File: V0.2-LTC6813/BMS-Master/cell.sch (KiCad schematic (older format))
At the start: 3 parts

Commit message: schematics 50% complete3d
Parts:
- added JP?: Jumper_NC_Dual-Device, symbol BMS-Master-rescue:Jumper_NC_Dual-Device
- added Q?: BSS138, Package_TO_SOT_SMD:SOT-23, symbol Transistor_FET:BSS138
- added R?: 10, Resistor_SMD:R_0603_1608Metric_Pad0.99x1.00mm_HandSolder, symbol Device:R
- added R?: 33, Resistor_SMD:R_0603_1608Metric_Pad0.99x1.00mm_HandSolder, symbol Device:R
- C?: value C -> 100n; Voltage (none) -> 100V
- R?: value 10 -> 100
- R?: value 33 -> R
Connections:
- net C+: now also JP?.3, Q?.2 (S); no longer R?.2
- net V-: now also R?.1; no longer C?.1
- new net: JP?.2, R?.2
- new net: JP?.1, Q?.1 (G)
- new net: Q?.3 (D), R?.2
- new net GND: C?.1
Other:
- moved on the sheet: C?

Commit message: Schematics 75% completed
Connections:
- net GND renamed GNDA
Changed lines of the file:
@@
 Wire Wire Line
 	5650 3950 5650 4750
+Wire Wire Line
+	3400 4800 3400 5000
+Wire Wire Line
+	3400 5000 2550 5000
 $Comp
-L power:GND #PWR?
-U 1 1 5C6DEC90
+L power:GNDA #PWR?
+U 1 1 5C8C20A9
 P 5650 4750
-AR Path="/5B4A196B/5B5115CC/5C6DEC90" Ref="#PWR?"  Part="1"
-AR Path="/5B4A196B/5B4FCC47/5C6DEC90" Ref="#PWR?"  Part="1"
-AR Path="/5B4A196B/5B4FD503/5C6DEC90" Ref="#PWR?"  Part="1"
-AR Path="/5B4A196B/5B50012A/5C6DEC90" Ref="#PWR?"  Part="1"
-AR Path="/5B4A196B/5B502FEF/5C6DEC90" Ref="#PWR?"  Part="1"
-AR Path="/5B4A196B/5B50355C/5C6DEC90" Ref="#PWR?"  Part="1"
-AR Path="/5B4A196B/5B504105/5C6DEC90" Ref="#PWR?"  Part="1"
-AR Path="/5B4A196B/5B504814/5C6DEC90" Ref="#PWR?"  Part="1"
-AR Path="/5B4A196B/5B5050BC/5C6DEC90" Ref="#PWR?"  Part="1"
-AR Path="/5B4A196B/5B50594B/5C6DEC90" Ref="#PWR?"  Part="1"
-AR Path="/5B4A196B/5B506BB1/5C6DEC90" Ref="#PWR?"  Part="1"
-AR Path="/5B4A196B/5B507536/5C6DEC90" Ref="#PWR?"  Part="1"
-AR Path="/5B4A196B/5B50804F/5C6DEC90" Ref="#PWR?"  Part="1"
-AR Path="/5B4A196B/5B508C6C/5C6DEC90" Ref="#PWR?"  Part="1"
-AR Path="/5B4A196B/5B509A8B/5C6DEC90" Ref="#PWR?"  Part="1"
-AR Path="/5B4A196B/5B50AABA/5C6DEC90" Ref="#PWR?"  Part="1"
-AR Path="/5B4A196B/5B50EED8/5C6DEC90" Ref="#PWR?"  Part="1"
-AR Path="/5B4A196B/5B510167/5C6DEC90" Ref="#PWR?"  Part="1"
 F 0 "#PWR?" H 5650 4500 50  0001 C CNN
-F 1 "GND" H 5655 4577 50  0000 C CNN
+F 1 "GNDA" H 5655 4577 50  0000 C CNN
 F 2 "" H 5650 4750 50  0001 C CNN
 F 3 "" H 5650 4750 50  0001 C CNN
@@
 	1    0    0    -1
 $EndComp
-Wire Wire Line
-	3400 4800 3400 5000
-Wire Wire Line
-	3400 5000 2550 5000
 $EndSCHEMATC

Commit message: Schematics 90% completed
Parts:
- removed R?: 10, Resistor_SMD:R_0603_1608Metric_Pad0.99x1.00mm_HandSolder, symbol Device:R
- JP21: renamed from JP?; footprint (none) -> Pin_Headers:Pin_Header_Straight_1x03_Pitch2.54mm
- gave numbers to parts that had none: 5

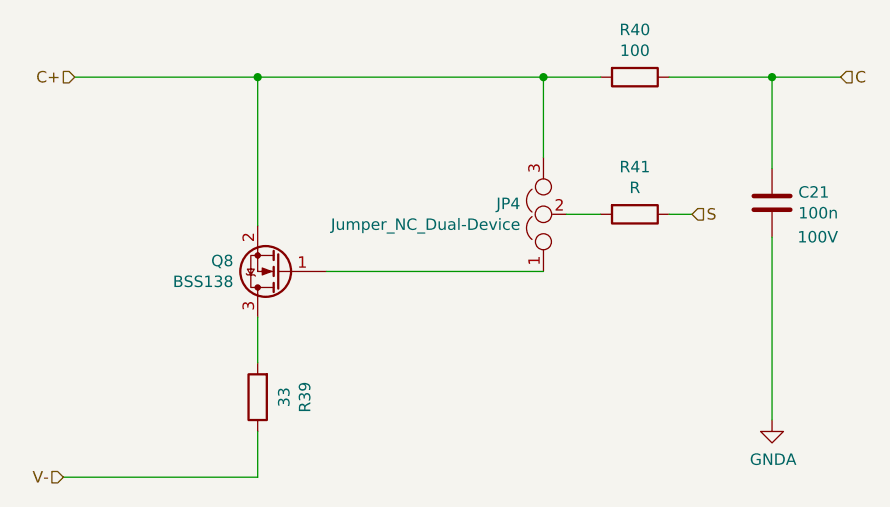
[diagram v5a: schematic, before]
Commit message: 92.5% schematics completed
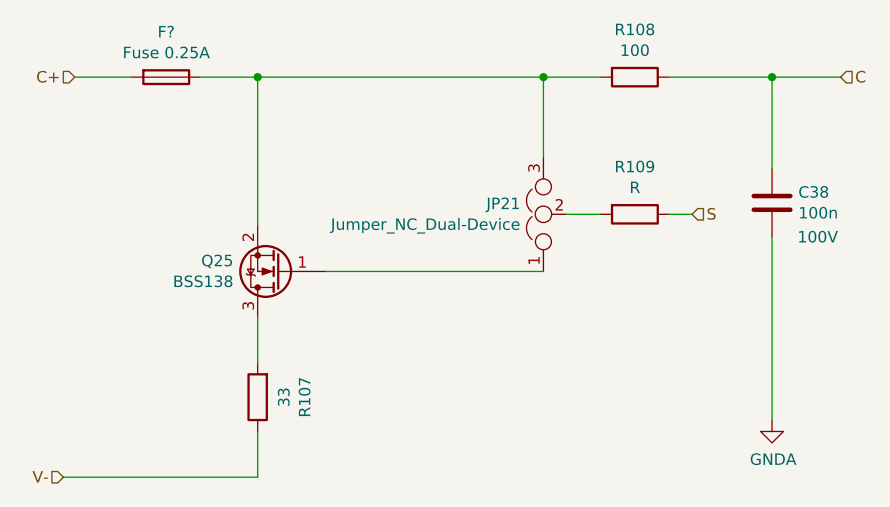
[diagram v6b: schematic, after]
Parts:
- added F?: Fuse 0.25A, Fuse_Holders_and_Fuses:Fuse_SMD1206_HandSoldering, symbol Device:Fuse
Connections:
- net C+: now also F?.2; no longer JP21.3, Q25.2 (S), R48.2
- new net: F?.1, JP21.3, Q25.2 (S), R48.2
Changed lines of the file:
@@
 AR Path="/5B4A196B/5B50EED8/5B4FCD0D" Ref="R100"  Part="1"
 AR Path="/5B4A196B/5B510167/5B4FCD0D" Ref="R104"  Part="1"
-F 0 "R40" V 4843 3250 50  0000 C CNN
+F 0 "R108" V 4843 3250 50  0000 C CNN
 F 1 "100" V 4934 3250 50  0000 C CNN
 F 2 "Resistor_SMD:R_0603_1608Metric_Pad0.99x1.00mm_HandSolder" V 4980 3250 50  0001 C CNN
@@
 AR Path="/5B4A196B/5B50EED8/5B4FCD15" Ref="C36"  Part="1"
 AR Path="/5B4A196B/5B510167/5B4FCD15" Ref="C37"  Part="1"
-F 0 "C21" H 5535 3754 50  0000 R CNN
+F 0 "C38" H 5535 3754 50  0000 R CNN
 F 1 "100n" H 5535 3845 50  0000 R CNN
 F 2 "Capacitor_SMD:C_0603_1608Metric_Pad0.99x1.00mm_HandSolder" H 5688 3650 50  0001 C CNN
@@
 AR Path="/5B4A196B/5B50EED8/5B4FCD21" Ref="R101"  Part="1"
 AR Path="/5B4A196B/5B510167/5B4FCD21" Ref="R105"  Part="1"
-F 0 "R41" V 4843 3850 50  0000 C CNN
+F 0 "R109" V 4843 3850 50  0000 C CNN
 F 1 "R" V 4934 3850 50  0000 C CNN
 F 2 "Resistor_SMD:R_0603_1608Metric_Pad0.99x1.00mm_HandSolder" V 4980 3850 50  0001 C CNN
@@
 AR Path="/5B4A196B/5B50EED8/5C6D5C4A" Ref="JP19"  Part="1"
 AR Path="/5B4A196B/5B510167/5C6D5C4A" Ref="JP20"  Part="1"
-F 0 "JP4" V 4696 3951 50  0000 L CNN
+F 0 "JP21" V 4696 3951 50  0000 L CNN
 F 1 "Jumper_NC_Dual-Device" V 4605 3951 50  0000 L CNN
 F 2 "Pin_Headers:Pin_Header_Straight_1x03_Pitch2.54mm" H 4650 3850 50  0001 C CNN
@@
 AR Path="/5B4A196B/5B50EED8/5C6D64D7" Ref="Q23"  Part="1"
 AR Path="/5B4A196B/5B510167/5C6D64D7" Ref="Q24"  Part="1"
-F 0 "Q8" H 3706 4054 50  0000 L CNN
+F 0 "Q25" H 3706 4054 50  0000 L CNN
 F 1 "BSS138" H 3706 4145 50  0000 L CNN
 F 2 "Package_TO_SOT_SMD:SOT-23" H 3700 4025 50  0001 L CIN
@@
 $EndComp
 Wire Wire Line
-	2600 3250 3400 3250
+	2600 3250 2850 3250
 Wire Wire Line
 	4650 3600 4650 3250
@@
 AR Path="/5B4A196B/5B50EED8/5C6D9E32" Ref="R99"  Part="1"
 AR Path="/5B4A196B/5B510167/5C6D9E32" Ref="R103"  Part="1"
-F 0 "R39" V 3193 4650 50  0000 C CNN
+F 0 "R107" V 3193 4650 50  0000 C CNN
 F 1 "33" V 3284 4650 50  0000 C CNN
 F 2 "Resistor_SMD:R_0603_1608Metric_Pad0.99x1.00mm_HandSolder" V 3330 4650 50  0001 C CNN
@@
 AR Path="/5B4A196B/5B510167/5C8C20A9" Ref="#PWR0170"  Part="1"
 AR Path="/5B4A196B/5B5115CC/5C8C20A9" Ref="#PWR0171"  Part="1"
-F 0 "#PWR0154" H 5650 4500 50  0001 C CNN
+F 0 "#PWR0171" H 5650 4500 50  0001 C CNN
 F 1 "GNDA" H 5655 4577 50  0000 C CNN
 F 2 "" H 5650 4750 50  0001 C CNN
@@
 Wire Wire Line
 	3400 4800 3400 5000
+Wire Wire Line
+	3150 3250 3400 3250
+$Comp
+L Device:Fuse F?
+U 1 1 5CDF9F6D
+P 3000 3250
+F 0 "F?" V 2803 3250 50  0000 C CNN
+F 1 "Fuse 0.25A" V 2894 3250 50  0000 C CNN
+F 2 "Fuse_Holders_and_Fuses:Fuse_SMD1206_HandSoldering" V 2930 3250 50  0001 C CNN
+F 3 "~" H 3000 3250 50  0001 C CNN
+	1    3000 3250
+	0    1    1    0
+$EndComp
 $EndSCHEMATC

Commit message: Schematics 99% completed
Only need to review everything &
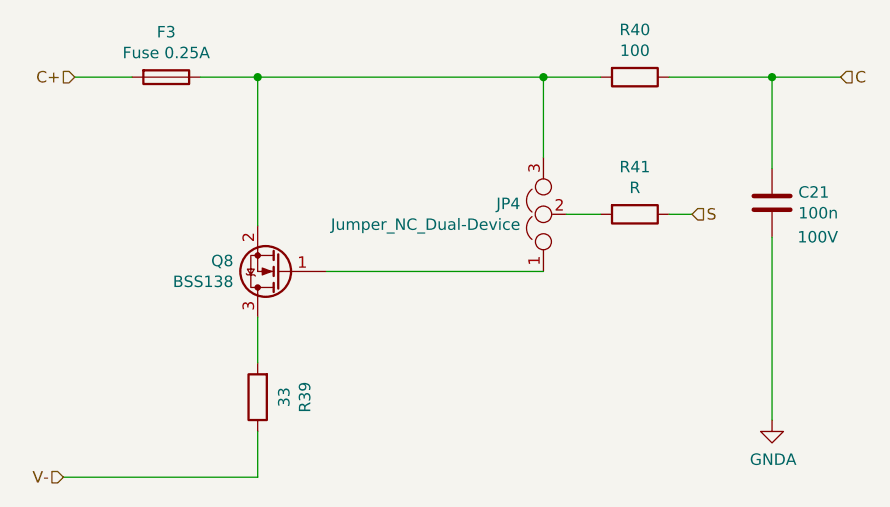
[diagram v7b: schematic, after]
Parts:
- gave numbers to parts that had none: 1
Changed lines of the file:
@@
 $Descr A4 11693 8268
 encoding utf-8
-Sheet 22 28
+Sheet 5 28
 Title ""
 Date ""
@@
 AR Path="/5B4A196B/5B50EED8/5B4FCD0D" Ref="R100"  Part="1"
 AR Path="/5B4A196B/5B510167/5B4FCD0D" Ref="R104"  Part="1"
-F 0 "R108" V 4843 3250 50  0000 C CNN
+F 0 "R40" V 4843 3250 50  0000 C CNN
 F 1 "100" V 4934 3250 50  0000 C CNN
 F 2 "Resistor_SMD:R_0603_1608Metric_Pad0.99x1.00mm_HandSolder" V 4980 3250 50  0001 C CNN
@@
 AR Path="/5B4A196B/5B50EED8/5B4FCD15" Ref="C36"  Part="1"
 AR Path="/5B4A196B/5B510167/5B4FCD15" Ref="C37"  Part="1"
-F 0 "C38" H 5535 3754 50  0000 R CNN
+F 0 "C21" H 5535 3754 50  0000 R CNN
 F 1 "100n" H 5535 3845 50  0000 R CNN
 F 2 "Capacitor_SMD:C_0603_1608Metric_Pad0.99x1.00mm_HandSolder" H 5688 3650 50  0001 C CNN
@@
 AR Path="/5B4A196B/5B50EED8/5B4FCD21" Ref="R101"  Part="1"
 AR Path="/5B4A196B/5B510167/5B4FCD21" Ref="R105"  Part="1"
-F 0 "R109" V 4843 3850 50  0000 C CNN
+F 0 "R41" V 4843 3850 50  0000 C CNN
 F 1 "R" V 4934 3850 50  0000 C CNN
 F 2 "Resistor_SMD:R_0603_1608Metric_Pad0.99x1.00mm_HandSolder" V 4980 3850 50  0001 C CNN
@@
 AR Path="/5B4A196B/5B50EED8/5C6D5C4A" Ref="JP19"  Part="1"
 AR Path="/5B4A196B/5B510167/5C6D5C4A" Ref="JP20"  Part="1"
-F 0 "JP21" V 4696 3951 50  0000 L CNN
+F 0 "JP4" V 4696 3951 50  0000 L CNN
 F 1 "Jumper_NC_Dual-Device" V 4605 3951 50  0000 L CNN
 F 2 "Pin_Headers:Pin_Header_Straight_1x03_Pitch2.54mm" H 4650 3850 50  0001 C CNN
@@
 AR Path="/5B4A196B/5B50EED8/5C6D64D7" Ref="Q23"  Part="1"
 AR Path="/5B4A196B/5B510167/5C6D64D7" Ref="Q24"  Part="1"
-F 0 "Q25" H 3706 4054 50  0000 L CNN
+F 0 "Q8" H 3706 4054 50  0000 L CNN
 F 1 "BSS138" H 3706 4145 50  0000 L CNN
 F 2 "Package_TO_SOT_SMD:SOT-23" H 3700 4025 50  0001 L CIN
@@
 AR Path="/5B4A196B/5B50EED8/5C6D9E32" Ref="R99"  Part="1"
 AR Path="/5B4A196B/5B510167/5C6D9E32" Ref="R103"  Part="1"
-F 0 "R107" V 3193 4650 50  0000 C CNN
+F 0 "R39" V 3193 4650 50  0000 C CNN
 F 1 "33" V 3284 4650 50  0000 C CNN
 F 2 "Resistor_SMD:R_0603_1608Metric_Pad0.99x1.00mm_HandSolder" V 3330 4650 50  0001 C CNN
@@
 AR Path="/5B4A196B/5B510167/5C8C20A9" Ref="#PWR0170"  Part="1"
 AR Path="/5B4A196B/5B5115CC/5C8C20A9" Ref="#PWR0171"  Part="1"
-F 0 "#PWR0171" H 5650 4500 50  0001 C CNN
+F 0 "#PWR0154" H 5650 4500 50  0001 C CNN
 F 1 "GNDA" H 5655 4577 50  0000 C CNN
 F 2 "" H 5650 4750 50  0001 C CNN
@@
 	3150 3250 3400 3250
 $Comp
-L Device:Fuse F?
+L Device:Fuse F3
 U 1 1 5CDF9F6D
 P 3000 3250
-F 0 "F?" V 2803 3250 50  0000 C CNN
+AR Path="/5B4A196B/5B4FCC47/5CDF9F6D" Ref="F3"  Part="1"
+AR Path="/5B4A196B/5B4FD503/5CDF9F6D" Ref="F4"  Part="1"
+AR Path="/5B4A196B/5B50012A/5CDF9F6D" Ref="F5"  Part="1"
+AR Path="/5B4A196B/5B502FEF/5CDF9F6D" Ref="F6"  Part="1"
+AR Path="/5B4A196B/5B50355C/5CDF9F6D" Ref="F7"  Part="1"
+AR Path="/5B4A196B/5B504105/5CDF9F6D" Ref="F8"  Part="1"
+AR Path="/5B4A196B/5B504814/5CDF9F6D" Ref="F9"  Part="1"
+AR Path="/5B4A196B/5B5050BC/5CDF9F6D" Ref="F10"  Part="1"
+AR Path="/5B4A196B/5B50594B/5CDF9F6D" Ref="F11"  Part="1"
+AR Path="/5B4A196B/5B506BB1/5CDF9F6D" Ref="F12"  Part="1"
+AR Path="/5B4A196B/5B507536/5CDF9F6D" Ref="F13"  Part="1"
+AR Path="/5B4A196B/5B50804F/5CDF9F6D" Ref="F14"  Part="1"
+AR Path="/5B4A196B/5B508C6C/5CDF9F6D" Ref="F15"  Part="1"
+AR Path="/5B4A196B/5B509A8B/5CDF9F6D" Ref="F16"  Part="1"
+AR Path="/5B4A196B/5B50AABA/5CDF9F6D" Ref="F17"  Part="1"
+AR Path="/5B4A196B/5B50EED8/5CDF9F6D" Ref="F18"  Part="1"
+AR Path="/5B4A196B/5B510167/5CDF9F6D" Ref="F19"  Part="1"
+AR Path="/5B4A196B/5B5115CC/5CDF9F6D" Ref="F20"  Part="1"
+F 0 "F3" V 2803 3250 50  0000 C CNN
 F 1 "Fuse 0.25A" V 2894 3250 50  0000 C CNN
 F 2 "Fuse_Holders_and_Fuses:Fuse_SMD1206_HandSoldering" V 2930 3250 50  0001 C CNN
